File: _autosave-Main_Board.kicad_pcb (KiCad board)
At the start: 2 copper layers, 90 x 90 mm, 62 parts, among them J1 DAC_12-bits, J2 Bias_Header, J3 Measurement_Header, Q1 Q_PNP_BCE, Q2 Q_NPN_BCE, U1 AD667, U2 LF356

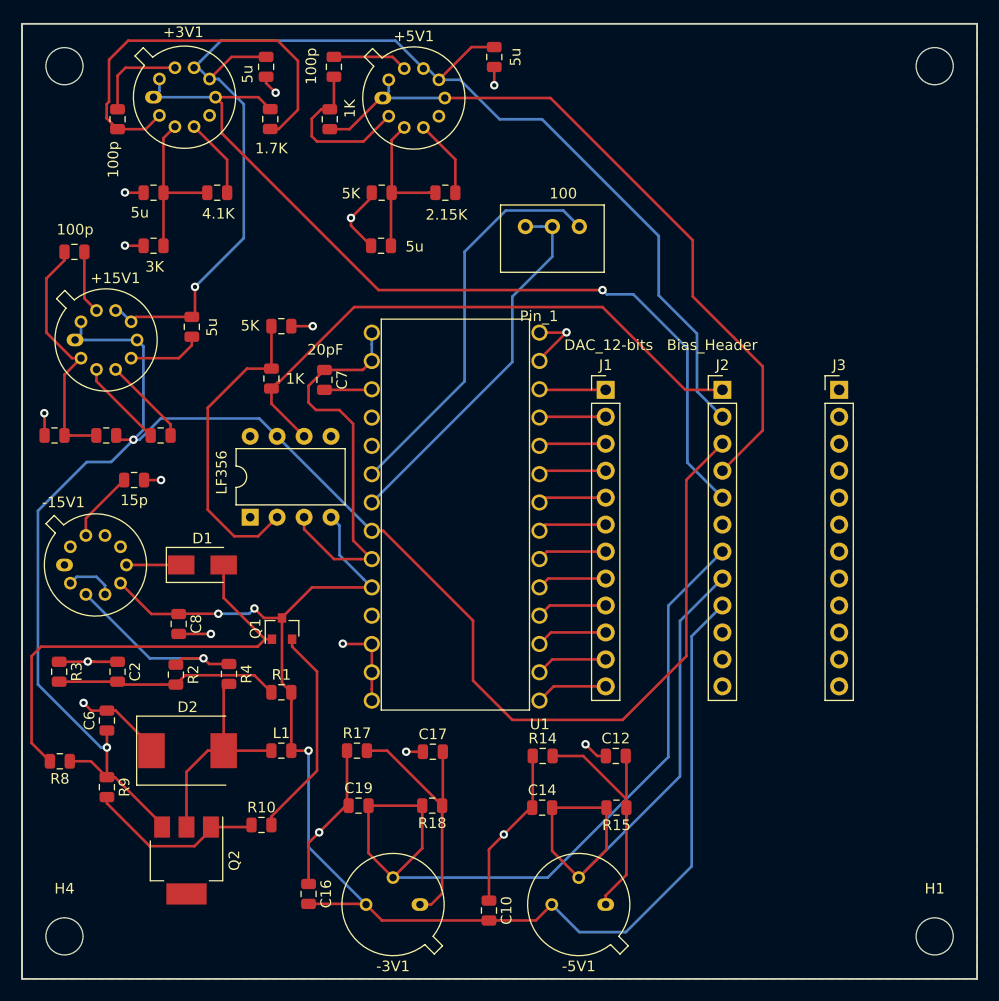
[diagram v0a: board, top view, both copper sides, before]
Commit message: Changing values to silk screen
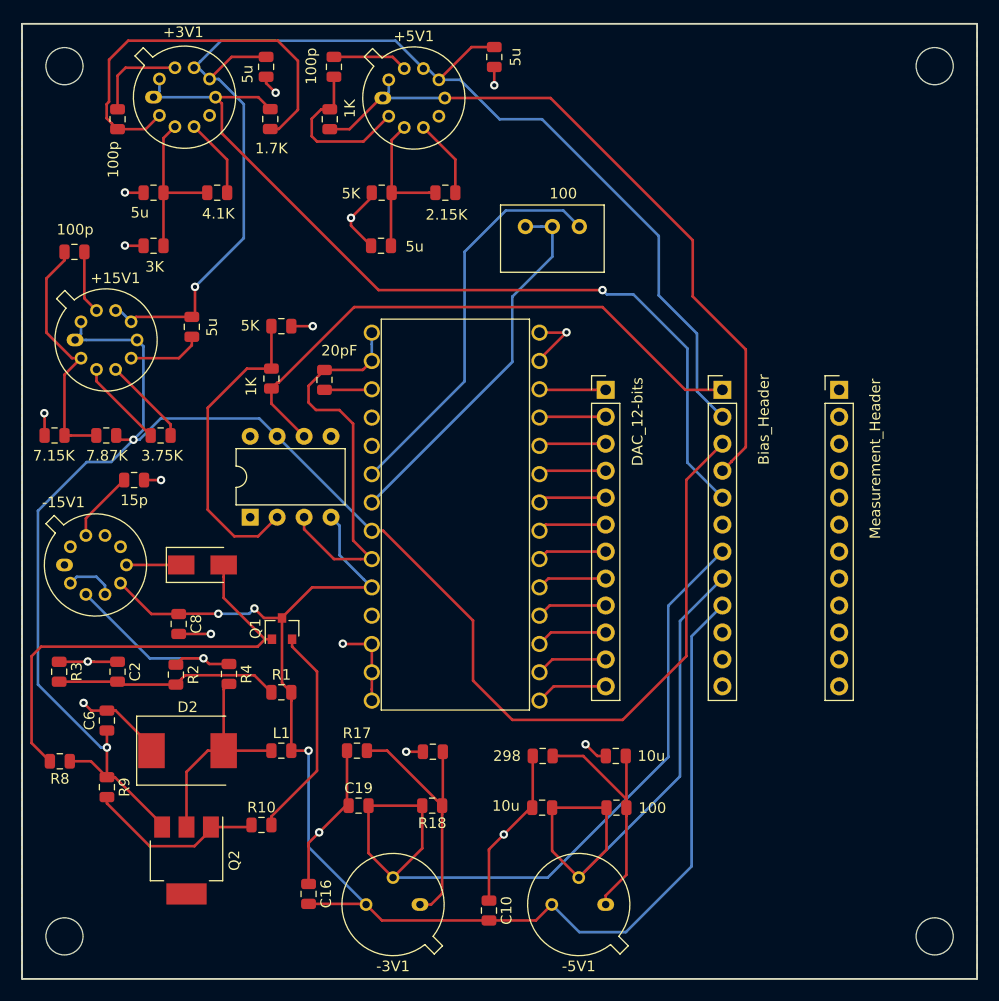
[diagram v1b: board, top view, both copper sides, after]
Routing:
- net /+5V: track 68.9 -> 67.6 mm
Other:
- board text removed: "Pin_1"
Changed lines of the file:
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@@
   (general
     (thickness 1.6)
-    (drawings 11)
-    (tracks 412)
+    (drawings 10)
+    (tracks 414)
     (zones 0)
     (modules 62)
@@
     (descr "Through hole straight pin header, 1x12, 2.54mm pitch, single row")
     (tags "Through hole pin header THT 1x12 2.54mm single row")
-    (fp_text reference J3 (at 0 -2.33) (layer F.SilkS)
-      (effects (font (size 1 1) (thickness 0.15)))
-    )
-    (fp_text value Measurement_Header (at 0 30.27) (layer F.Fab)
+    (fp_text reference J3 (at 0 -2.33) (layer F.Fab)
+      (effects (font (size 1 1) (thickness 0.15)))
+    )
+    (fp_text value Measurement_Header (at 3.4 6.5 90) (layer F.SilkS)
       (effects (font (size 1 1) (thickness 0.15)))
     )
@@
   (module REDD_main_board:AD667_12-bit_DAC (layer F.Cu)
     (at 47.5 119 270)
-    (fp_text reference U1 (at 28.0162 -13.2842 180) (layer F.SilkS)
-      (effects (font (size 1 1) (thickness 0.15)))
-    )
-    (fp_text value AD667 (at -11.43 -11.9634 180) (layer F.Fab)
+    (fp_text reference U1 (at 25 -10.7 180) (layer F.Fab)
+      (effects (font (size 1 1) (thickness 0.15)))
+    )
+    (fp_text value AD667 (at -2.3 -4.4 180) (layer F.Fab)
       (effects (font (size 1 1) (thickness 0.15)))
     )
@@
       (effects (font (size 1 1) (thickness 0.15)))
     )
-    (fp_text value LF356 (at 4.2164 -2.6924 90) (layer F.SilkS)
+    (fp_text value LF356 (at 4.2164 -2.6924 90) (layer F.Fab)
       (effects (font (size 1 1) (thickness 0.15)))
     )
@@
     (tags resistor)
     (attr smd)
-    (fp_text reference R22 (at 0 -1.65 90) (layer F.Fab)
-      (effects (font (size 1 1) (thickness 0.15)))
-    )
-    (fp_text value 1K (at -0.0231 2.2352 180) (layer F.SilkS)
+    (fp_text reference R22 (at -0.2625 1.9 90) (layer F.Fab)
+      (effects (font (size 1 1) (thickness 0.15)))
+    )
+    (fp_text value 1K (at -0.7625 -1.9 270) (layer F.SilkS)
       (effects (font (size 1 1) (thickness 0.15)))
     )
@@
     (tags capacitor)
     (attr smd)
-    (fp_text reference C7 (at 0 -1.65 90) (layer F.SilkS)
-      (effects (font (size 1 1) (thickness 0.15)))
-    )
-    (fp_text value 20pF (at -2.8471 -0.0762 180) (layer F.SilkS)
+    (fp_text reference C7 (at 0 -1.65 90) (layer F.Fab)
+      (effects (font (size 1 1) (thickness 0.15)))
+    )
+    (fp_text value 20pF (at -2.7625 -1.4 180) (layer F.SilkS)
       (effects (font (size 1 1) (thickness 0.15)))
     )
@@
     (tags capacitor)
     (attr smd)
-    (fp_text reference C4 (at 0 -1.65) (layer F.Fab)
+    (fp_text reference C4 (at -2.7625 0) (layer F.Fab)
       (effects (font (size 1 1) (thickness 0.15)))
     )
@@
     (tags "mounting hole 3.5mm no annular")
     (attr virtual)
-    (fp_text reference H4 (at 0 -4.5) (layer F.SilkS)
+    (fp_text reference H4 (at 0 -4.5) (layer F.Fab)
       (effects (font (size 1 1) (thickness 0.15)))
     )
@@
     (tags "mounting hole 3.5mm no annular")
     (attr virtual)
-    (fp_text reference H1 (at 0 -4.5) (layer F.SilkS)
+    (fp_text reference H1 (at 0 -4.5) (layer F.Fab)
       (effects (font (size 1 1) (thickness 0.15)))
     )
@@
     (descr "Through hole straight pin header, 1x12, 2.54mm pitch, single row")
     (tags "Through hole pin header THT 1x12 2.54mm single row")
-    (fp_text reference J2 (at 0 -2.33) (layer F.SilkS)
-      (effects (font (size 1 1) (thickness 0.15)))
-    )
-    (fp_text value Bias_Header (at -0.9652 -4.2164) (layer F.SilkS)
+    (fp_text reference J2 (at 0 -2.33) (layer F.Fab)
+      (effects (font (size 1 1) (thickness 0.15)))
+    )
+    (fp_text value Bias_Header (at 3.9 2.8 90) (layer F.SilkS)
       (effects (font (size 1 1) (thickness 0.15)))
     )
@@
     (descr "Through hole straight pin header, 1x12, 2.54mm pitch, single row")
     (tags "Through hole pin header THT 1x12 2.54mm single row")
-    (fp_text reference J1 (at 0 -2.33) (layer F.SilkS)
-      (effects (font (size 1 1) (thickness 0.15)))
-    )
-    (fp_text value DAC_12-bits (at 0.2794 -4.2164) (layer F.SilkS)
+    (fp_text reference J1 (at 0 -2.33) (layer F.Fab)
+      (effects (font (size 1 1) (thickness 0.15)))
+    )
+    (fp_text value DAC_12-bits (at 3 3 90) (layer F.SilkS)
       (effects (font (size 1 1) (thickness 0.15)))
     )
@@
     (tags "Diode SMA (DO-214AC)")
     (attr smd)
-    (fp_text reference D1 (at 0 -2.5) (layer F.SilkS)
+    (fp_text reference D1 (at 0 -2.5) (layer F.Fab)
       (effects (font (size 1 1) (thickness 0.15)))
     )
@@
     (tags resistor)
     (attr smd)
-    (fp_text reference R20 (at 1.5625 3.8) (layer F.Fab)
-      (effects (font (size 1 1) (thickness 0.15)))
-    )
-    (fp_text value 7.15K (at 0 -4) (layer F.Fab)
+    (fp_text reference R20 (at 1.4625 3.2) (layer F.Fab)
+      (effects (font (size 1 1) (thickness 0.15)))
+    )
+    (fp_text value 7.15K (at 0.0625 -1.9) (layer F.SilkS)
       (effects (font (size 1 1) (thickness 0.15)))
     )
@@
     (tags resistor)
     (attr smd)
-    (fp_text reference R19 (at 0 -1.65) (layer F.Fab)
-      (effects (font (size 1 1) (thickness 0.15)))
-    )
-    (fp_text value 7.87K (at 0 1.65) (layer F.Fab)
+    (fp_text reference R19 (at 0.0375 1.8) (layer F.Fab)
+      (effects (font (size 1 1) (thickness 0.15)))
+    )
+    (fp_text value 7.87K (at -0.0625 -1.9) (layer F.SilkS)
       (effects (font (size 1 1) (thickness 0.15)))
     )
@@
     (tags resistor)
     (attr smd)
-    (fp_text reference R16 (at 0 -1.65) (layer F.Fab)
-      (effects (font (size 1 1) (thickness 0.15)))
-    )
-    (fp_text value 3.75K (at 0 1.65) (layer F.Fab)
+    (fp_text reference R16 (at 0.1625 1.7) (layer F.Fab)
+      (effects (font (size 1 1) (thickness 0.15)))
+    )
+    (fp_text value 3.75K (at -0.1375 -1.9) (layer F.SilkS)
       (effects (font (size 1 1) (thickness 0.15)))
     )
@@
     (tags resistor)
     (attr smd)
-    (fp_text reference R15 (at 0 -1.65) (layer F.SilkS)
-      (effects (font (size 1 1) (thickness 0.15)))
-    )
-    (fp_text value 100 (at 0 1.65) (layer F.Fab)
+    (fp_text reference R15 (at 0 -1.65) (layer F.Fab)
+      (effects (font (size 1 1) (thickness 0.15)))
+    )
+    (fp_text value 100 (at -3.3867 -0.0286) (layer F.SilkS)
       (effects (font (size 1 1) (thickness 0.15)))
     )
@@
     (tags resistor)
     (attr smd)
-    (fp_text reference R14 (at 0 -1.65) (layer F.SilkS)
-      (effects (font (size 1 1) (thickness 0.15)))
-    )
-    (fp_text value 298 (at 0 1.65) (layer F.Fab)
+    (fp_text reference R14 (at 0 -1.65) (layer F.Fab)
+      (effects (font (size 1 1) (thickness 0.15)))
+    )
+    (fp_text value 298 (at -3.3625 0) (layer F.SilkS)
       (effects (font (size 1 1) (thickness 0.15)))
     )
@@
     (tags capacitor)
     (attr smd)
-    (fp_text reference C17 (at 0 -1.65) (layer F.SilkS)
+    (fp_text reference C17 (at 0 -1.65) (layer F.Fab)
       (effects (font (size 1 1) (thickness 0.15)))
     )
@@
     (tags capacitor)
     (attr smd)
-    (fp_text reference C14 (at 0 -1.65) (layer F.SilkS)
-      (effects (font (size 1 1) (thickness 0.15)))
-    )
-    (fp_text value 10u (at 0 1.65) (layer F.Fab)
+    (fp_text reference C14 (at 0 -1.65) (layer F.Fab)
+      (effects (font (size 1 1) (thickness 0.15)))
+    )
+    (fp_text value 10u (at -3.4133 -0.1714) (layer F.SilkS)
       (effects (font (size 1 1) (thickness 0.15)))
     )
@@
     (tags capacitor)
     (attr smd)
-    (fp_text reference C12 (at 0 -1.65) (layer F.SilkS)
-      (effects (font (size 1 1) (thickness 0.15)))
-    )
-    (fp_text value 10u (at 0 1.65) (layer F.Fab)
+    (fp_text reference C12 (at 0 -1.65) (layer F.Fab)
+      (effects (font (size 1 1) (thickness 0.15)))
+    )
+    (fp_text value 10u (at 3.3492 0) (layer F.SilkS)
       (effects (font (size 1 1) (thickness 0.15)))
     )
@@
   (gr_line (start 12 171) (end 102 171) (layer F.SilkS) (width 0.15))
   (gr_line (start 12 81) (end 12 171) (layer F.SilkS) (width 0.15))
-  (gr_text "Pin_1\n" (at 60.7172 108.559) (layer F.SilkS)
-    (effects (font (size 1 1) (thickness 0.15)))
-  )
   (via (at 35.9 87.5) (size 0.8) (drill 0.4) (layers F.Cu B.Cu) (net 1))
   (segment (start 35 86) (end 35 86.6) (width 0.25) (layer F.Cu) (net 1))
@@
   (segment (start 42.8625 90.9375) (end 45.8 88) (width 0.25) (layer F.Cu) (net 9))
   (segment (start 41 90.9375) (end 42.8625 90.9375) (width 0.25) (layer F.Cu) (net 9))
-  (segment (start 51.84 88) (end 61.8 88) (width 0.25) (layer F.Cu) (net 9))
-  (segment (start 61.8 88) (end 75.2 101.4) (width 0.25) (layer F.Cu) (net 9))
-  (segment (start 75.2 101.4) (end 75.2 106.7) (width 0.25) (layer F.Cu) (net 9))
-  (segment (start 75.2 106.7) (end 81.8 113.3) (width 0.25) (layer F.Cu) (net 9))
-  (segment (start 81.8 119.32) (end 78 123.12) (width 0.25) (layer F.Cu) (net 9))
-  (segment (start 81.8 113.3) (end 81.8 119.32) (width 0.25) (layer F.Cu) (net 9))
+  (segment (start 61.8 88) (end 51.84 88) (width 0.25) (layer F.Cu) (net 9))
+  (segment (start 75.2 101.4) (end 61.8 88) (width 0.25) (layer F.Cu) (net 9))
+  (segment (start 78.849999 122.250001) (end 80.2 120.9) (width 0.25) (layer F.Cu) (net 9))
+  (segment (start 80.2 120.9) (end 80.2 111.7) (width 0.25) (layer F.Cu) (net 9))
+  (segment (start 80.2 111.7) (end 75.2 106.7) (width 0.25) (layer F.Cu) (net 9))
+  (segment (start 75.2 106.7) (end 75.2 101.4) (width 0.25) (layer F.Cu) (net 9))
+  (segment (start 78.849999 122.270001) (end 78 123.12) (width 0.25) (layer F.Cu) (net 9))
+  (segment (start 78.849999 122.250001) (end 78.849999 122.270001) (width 0.25) (layer F.Cu) (net 9))
   (segment (start 24.94907 87.36613) (end 24.3914 87.9238) (width 0.25) (layer B.Cu) (net 10))
   (segment (start 24.94907 86.207467) (end 24.94907 87.36613) (width 0.25) (layer B.Cu) (net 10))
